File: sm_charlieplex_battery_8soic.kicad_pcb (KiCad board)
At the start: 2 copper layers, 12 x 12 mm, 14 parts, among them SW1 SW_Push, U1 ATtiny10-TS

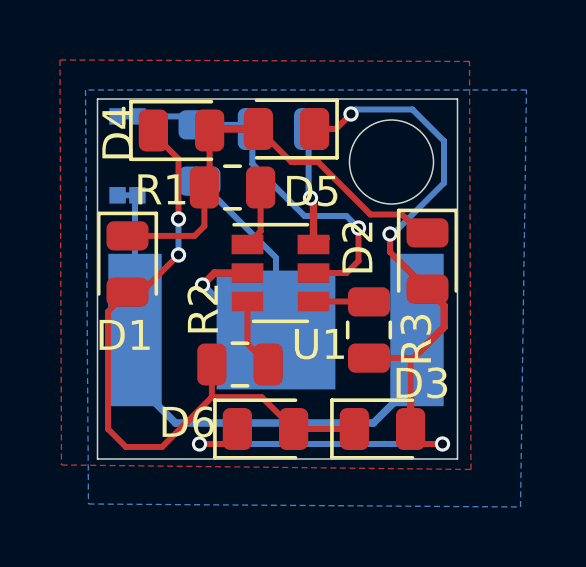
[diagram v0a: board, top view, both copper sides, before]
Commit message: Reformat to use ATTiny402
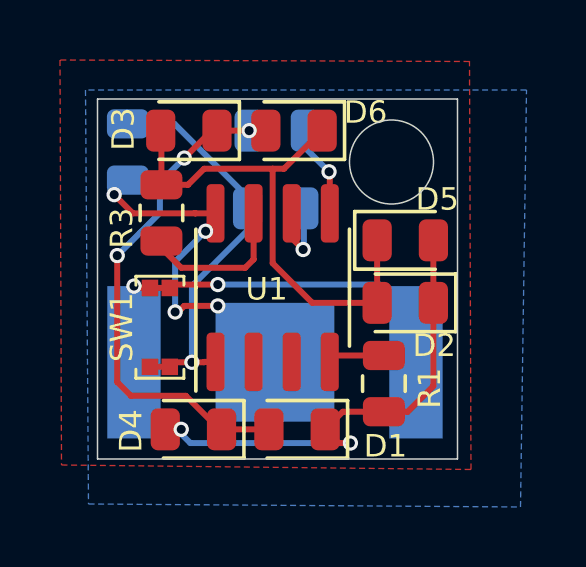
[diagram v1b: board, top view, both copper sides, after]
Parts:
- C1: value 4.7uF -> 0.1uF
- R2: moved to B.Cu
- SW1: moved to F.Cu
- U1: value ATtiny10-TS -> ATtiny402-SS; footprint Package_TO_SOT_SMD:SOT-23-6 -> Package_SO:SOIC-8_3.9x4.9mm_P1.27mm
- moved D3 11.9 mm to (167.9, 105.1), turned to 180 degrees
- moved D6 9.99 mm to (171.4, 105.1), turned to 180 degrees
- moved D4 9.97 mm to (168.1, 115.0), turned to 180 degrees
- moved R1 8.26 mm to (174.4, 113.5), turned to 90 degrees
- moved R3 7.94 mm to (167.0, 107.8), turned to 270 degrees
- moved D1 7.89 mm to (171.6, 115.0), turned to 180 degrees
- moved R2 7.89 mm to (170.9, 105.1)
- moved SW1 5.81 mm to (167.0, 111.6), turned to 270 degrees
- moved D5 5.43 mm to (175.2, 108.7), turned to 0 degrees
- moved R4 2.65 mm to (170.8, 107.6)
- moved C1 2.39 mm to (165.9, 105.8)
- moved D2 1.58 mm to (175.2, 110.8), turned to 180 degrees
- moved BT1 1.08 mm to (170.8, 112.8)
- moved U1 0.55 mm to (170.7, 110.3), turned to 90 degrees
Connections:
- U1 pad 1: Net-(R1-Pad2) -> Net-(C1-Pad1)
- U1 pad 2: /GND -> Net-(U1-Pad2)
- U1 pad 3: Net-(R2-Pad2) -> Net-(U1-Pad3)
- U1 pad 4: Net-(R3-Pad2) -> Net-(R1-Pad2)
- U1 pad 5: Net-(C1-Pad1) -> Net-(R2-Pad2)
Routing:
- net /+3V: track 33.1 -> 13.9 mm, vias 0 -> 2
- net Net-(D2-Pad2): track 28.9 -> 17.2 mm, vias 4 -> 0
- net /GND: track 14.4 -> 9.68 mm, vias 1 -> 4
- net Net-(D1-Pad2): track 22.5 -> 18.6 mm, vias 2 -> 3
- net Net-(R3-Pad2): track 2.17 -> 5.76 mm
- net Net-(D1-Pad1): track 14.7 -> 16.5 mm, vias 0 -> 2
- net Net-(R4-Pad2): track 4.37 -> 2.74 mm
- net Net-(R2-Pad2): track 2.38 -> 3.10 mm, vias 0 -> 1
- added copper zone on B.Cu, net /GND
- added copper zone on F.Cu, net /GND
- removed copper zone on B.Cu, net (none)
- removed copper zone on F.Cu, net (none)
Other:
- board text added: "WM v1.1.2 12/07/19"
- board text removed: "WM v1.1.1 09/17/19"

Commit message: Some changes
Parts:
- U1: value ATtiny402-SS -> ATtiny13A-SSU
- moved U1 0.05 mm to (170.7, 110.2), turned to 270 degrees
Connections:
- U1 pad 1: Net-(C1-Pad1) -> Net-(R4-Pad2)
- U1 pad 2: Net-(U1-Pad2) -> Net-(R3-Pad2)
- U1 pad 4: Net-(R1-Pad2) -> /GND
- U1 pad 5: Net-(R2-Pad2) -> Net-(U1-Pad5)
- U1 pad 6: Net-(R4-Pad2) -> Net-(R1-Pad2)
- U1 pad 7: Net-(R3-Pad2) -> Net-(R2-Pad2)
- U1 pad 8: /GND -> Net-(C1-Pad1)
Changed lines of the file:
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@@
   )
   (setup
-    (last_trace_width 0.2)
+    (last_trace_width 0.25)
     (user_trace_width 0.2)
     (trace_clearance 0.2)
@@
   (net 10 "Net-(C1-Pad1)")
   (net 11 "Net-(U1-Pad3)")
-  (net 12 "Net-(U1-Pad2)")
+  (net 12 "Net-(U1-Pad5)")
   (net_class Default "This is the default net class."
     (clearance 0.2)
@@
     (add_net "Net-(R3-Pad2)")
     (add_net "Net-(R4-Pad2)")
-    (add_net "Net-(U1-Pad2)")
     (add_net "Net-(U1-Pad3)")
+    (add_net "Net-(U1-Pad5)")
+  )
+  (module Package_SO:SOIC-8_3.9x4.9mm_P1.27mm (layer F.Cu)
+    (at 170.7388 110.236 270)
+    (descr "SOIC, 8 Pin (JEDEC MS-012AA, https://www.analog.com/media/en/package-pcb-resources/package/pkg_pdf/soic_narrow-r/r_8.pdf), generated with kicad-footprint-generator ipc_gullwing_generator.py")
+    (tags "SOIC SO")
+    (attr smd)
+    (fp_text reference U1 (at 0 -3.4 90) (layer F.SilkS)
+      (effects (font (size 1 1) (thickness 0.15)))
+    )
+    (fp_text value ATtiny13A-SSU (at 0 3.4 90) (layer F.Fab)
+      (effects (font (size 1 1) (thickness 0.15)))
+    )
+    (fp_text user %R (at 0 0 90) (layer F.Fab)
+      (effects (font (size 0.98 0.98) (thickness 0.15)))
+    )
+    (fp_line (start 3.7 -2.7) (end -3.7 -2.7) (layer F.CrtYd) (width 0.05))
+    (fp_line (start 3.7 2.7) (end 3.7 -2.7) (layer F.CrtYd) (width 0.05))
+    (fp_line (start -3.7 2.7) (end 3.7 2.7) (layer F.CrtYd) (width 0.05))
+    (fp_line (start -3.7 -2.7) (end -3.7 2.7) (layer F.CrtYd) (width 0.05))
+    (fp_line (start -1.95 -1.475) (end -0.975 -2.45) (layer F.Fab) (width 0.1))
+    (fp_line (start -1.95 2.45) (end -1.95 -1.475) (layer F.Fab) (width 0.1))
+    (fp_line (start 1.95 2.45) (end -1.95 2.45) (layer F.Fab) (width 0.1))
+    (fp_line (start 1.95 -2.45) (end 1.95 2.45) (layer F.Fab) (width 0.1))
+    (fp_line (start -0.975 -2.45) (end 1.95 -2.45) (layer F.Fab) (width 0.1))
+    (fp_line (start 0 -2.56) (end -3.45 -2.56) (layer F.SilkS) (width 0.12))
+    (fp_line (start 0 -2.56) (end 1.95 -2.56) (layer F.SilkS) (width 0.12))
+    (fp_line (start 0 2.56) (end -1.95 2.56) (layer F.SilkS) (width 0.12))
+    (fp_line (start 0 2.56) (end 1.95 2.56) (layer F.SilkS) (width 0.12))
+    (pad 8 smd roundrect (at 2.475 -1.905 270) (size 1.95 0.6) (layers F.Cu F.Paste F.Mask) (roundrect_rratio 0.25)
+      (net 10 "Net-(C1-Pad1)"))
+    (pad 7 smd roundrect (at 2.475 -0.635 270) (size 1.95 0.6) (layers F.Cu F.Paste F.Mask) (roundrect_rratio 0.25)
+      (net 6 "Net-(R2-Pad2)"))
+    (pad 6 smd roundrect (at 2.475 0.635 270) (size 1.95 0.6) (layers F.Cu F.Paste F.Mask) (roundrect_rratio 0.25)
+      (net 5 "Net-(R1-Pad2)"))
+    (pad 5 smd roundrect (at 2.475 1.905 270) (size 1.95 0.6) (layers F.Cu F.Paste F.Mask) (roundrect_rratio 0.25)
+      (net 12 "Net-(U1-Pad5)"))
+    (pad 4 smd roundrect (at -2.475 1.905 270) (size 1.95 0.6) (layers F.Cu F.Paste F.Mask) (roundrect_rratio 0.25)
+      (net 4 /GND))
+    (pad 3 smd roundrect (at -2.475 0.635 270) (size 1.95 0.6) (layers F.Cu F.Paste F.Mask) (roundrect_rratio 0.25)
+      (net 11 "Net-(U1-Pad3)"))
+    (pad 2 smd roundrect (at -2.475 -0.635 270) (size 1.95 0.6) (layers F.Cu F.Paste F.Mask) (roundrect_rratio 0.25)
+      (net 7 "Net-(R3-Pad2)"))
+    (pad 1 smd roundrect (at -2.475 -1.905 270) (size 1.95 0.6) (layers F.Cu F.Paste F.Mask) (roundrect_rratio 0.25)
+      (net 8 "Net-(R4-Pad2)"))
+    (model ${KISYS3DMOD}/Package_SO.3dshapes/SOIC-8_3.9x4.9mm_P1.27mm.wrl
+      (at (xyz 0 0 0))
+      (scale (xyz 1 1 1))
+      (rotate (xyz 0 0 0))
+    )
   )
   (module Battery:BatteryHolder_Keystone_2998_621_6.8x2.2mm (layer B.Cu)
@@
     (pad 2 smd rect (at 0 0) (size 3.96 3.96) (layers B.Cu B.Paste B.Mask)
       (net 4 /GND))
-  )
-  (module Package_SO:SOIC-8_3.9x4.9mm_P1.27mm (layer F.Cu)
-    (at 170.7388 110.2868 90)
-    (descr "SOIC, 8 Pin (JEDEC MS-012AA, https://www.analog.com/media/en/package-pcb-resources/package/pkg_pdf/soic_narrow-r/r_8.pdf), generated with kicad-footprint-generator ipc_gullwing_generator.py")
-    (tags "SOIC SO")
-    (attr smd)
-    (fp_text reference U1 (at -0.0508 -0.2032 180) (layer F.SilkS)
-      (effects (font (size 0.75 0.75) (thickness 0.1)))
-    )
-    (fp_text value ATtiny402-SS (at 0 3.4 90) (layer F.Fab)
-      (effects (font (size 1 1) (thickness 0.15)))
-    )
-    (fp_line (start 0 2.56) (end 1.95 2.56) (layer F.SilkS) (width 0.12))
-    (fp_line (start 0 2.56) (end -1.95 2.56) (layer F.SilkS) (width 0.12))
-    (fp_line (start 0 -2.56) (end 1.95 -2.56) (layer F.SilkS) (width 0.12))
-    (fp_line (start 0 -2.56) (end -3.45 -2.56) (layer F.SilkS) (width 0.12))
-    (fp_line (start -0.975 -2.45) (end 1.95 -2.45) (layer F.Fab) (width 0.1))
-    (fp_line (start 1.95 -2.45) (end 1.95 2.45) (layer F.Fab) (width 0.1))
-    (fp_line (start 1.95 2.45) (end -1.95 2.45) (layer F.Fab) (width 0.1))
-    (fp_line (start -1.95 2.45) (end -1.95 -1.475) (layer F.Fab) (width 0.1))
-    (fp_line (start -1.95 -1.475) (end -0.975 -2.45) (layer F.Fab) (width 0.1))
-    (fp_line (start -3.7 -2.7) (end -3.7 2.7) (layer F.CrtYd) (width 0.05))
-    (fp_line (start -3.7 2.7) (end 3.7 2.7) (layer F.CrtYd) (width 0.05))
-    (fp_line (start 3.7 2.7) (end 3.7 -2.7) (layer F.CrtYd) (width 0.05))
-    (fp_line (start 3.7 -2.7) (end -3.7 -2.7) (layer F.CrtYd) (width 0.05))
-    (fp_text user %R (at 0 0 90) (layer F.Fab)
-      (effects (font (size 0.98 0.98) (thickness 0.15)))
-    )
-    (pad 1 smd roundrect (at -2.475 -1.905 90) (size 1.95 0.6) (layers F.Cu F.Paste F.Mask) (roundrect_rratio 0.25)
-      (net 10 "Net-(C1-Pad1)"))
-    (pad 2 smd roundrect (at -2.475 -0.635 90) (size 1.95 0.6) (layers F.Cu F.Paste F.Mask) (roundrect_rratio 0.25)
-      (net 12 "Net-(U1-Pad2)"))
-    (pad 3 smd roundrect (at -2.475 0.635 90) (size 1.95 0.6) (layers F.Cu F.Paste F.Mask) (roundrect_rratio 0.25)
-      (net 11 "Net-(U1-Pad3)"))
-    (pad 4 smd roundrect (at -2.475 1.905 90) (size 1.95 0.6) (layers F.Cu F.Paste F.Mask) (roundrect_rratio 0.25)
-      (net 5 "Net-(R1-Pad2)"))
-    (pad 5 smd roundrect (at 2.475 1.905 90) (size 1.95 0.6) (layers F.Cu F.Paste F.Mask) (roundrect_rratio 0.25)
-      (net 6 "Net-(R2-Pad2)"))
-    (pad 6 smd roundrect (at 2.475 0.635 90) (size 1.95 0.6) (layers F.Cu F.Paste F.Mask) (roundrect_rratio 0.25)
-      (net 8 "Net-(R4-Pad2)"))
-    (pad 7 smd roundrect (at 2.475 -0.635 90) (size 1.95 0.6) (layers F.Cu F.Paste F.Mask) (roundrect_rratio 0.25)
-      (net 7 "Net-(R3-Pad2)"))
-    (pad 8 smd roundrect (at 2.475 -1.905 90) (size 1.95 0.6) (layers F.Cu F.Paste F.Mask) (roundrect_rratio 0.25)
-      (net 4 /GND))
-    (model ${KISYS3DMOD}/Package_SO.3dshapes/SOIC-8_3.9x4.9mm_P1.27mm.wrl
-      (at (xyz 0 0 0))
-      (scale (xyz 1 1 1))
-      (rotate (xyz 0 0 0))
-    )
   )
   (module Button_Switch_SMD:SW_Push_2.6x1.6x0.53mm_EVP-BB2A9B000 (layer F.Cu)
@@
   (gr_line (start 176.9 104) (end 176.9 116) (layer Edge.Cuts) (width 0.05))
   (gr_line (start 164.9 104) (end 176.9 104) (layer Edge.Cuts) (width 0.05))
-  (via (at 168.91 110.8964) (size 0.51) (drill 0.3) (layers F.Cu B.Cu) (net 4))
   (segment (start 173.0756 114.4247) (end 172.4891 115.0112) (width 0.2) (layer F.Cu) (net 1))
   (segment (start 174.4472 114.4247) (end 173.0756 114.4247) (width 0.2) (layer F.Cu) (net 1))
@@
   (segment (start 168.4528 106.3244) (end 170.7388 106.3244) (width 0.2) (layer F.Cu) (net 3))
   (segment (start 170.7388 106.3244) (end 171.1175 106.3244) (width 0.2) (layer F.Cu) (net 3))
+  (via (at 168.91 110.8964) (size 0.51) (drill 0.3) (layers F.Cu B.Cu) (net 4))
   (segment (start 168.8338 107.8118) (end 168.1622 107.8118) (width 0.2) (layer F.Cu) (net 4))
   (segment (start 168.1622 107.8118) (end 168.148 107.7976) (width 0.2) (layer F.Cu) (net 4))
